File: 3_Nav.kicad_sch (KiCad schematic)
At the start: 36 parts, among them J401 GNSS, Q401 Q_NMOS, SW401 SW_Push, SW402 SW_Push, U401 STM32F446VETx, Y401 YXC YSX321SL

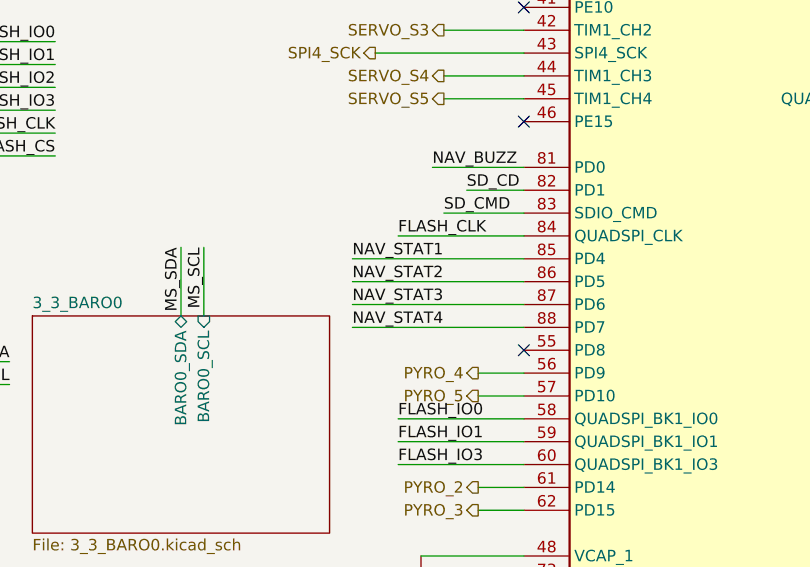
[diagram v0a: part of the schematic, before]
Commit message: Continued laying out traces
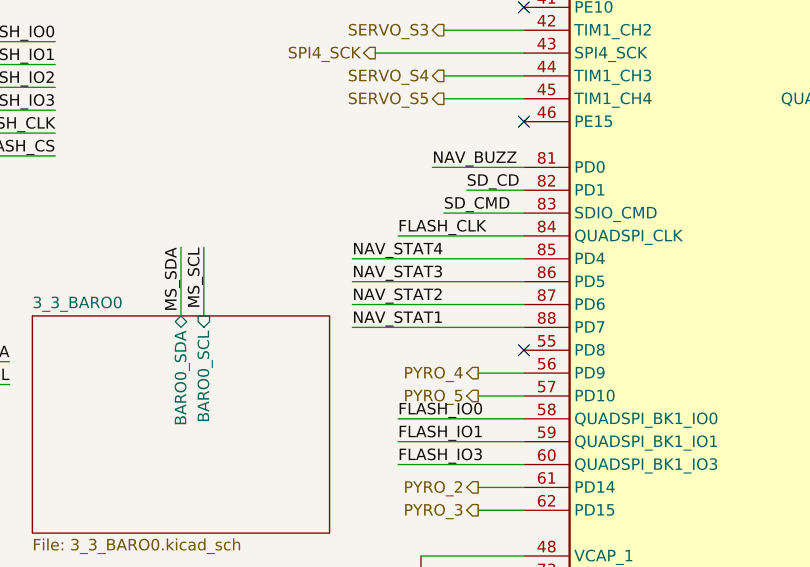
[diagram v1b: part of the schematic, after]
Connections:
- net NAV_STAT1: now also U401.88 (PD7); no longer U401.85 (PD4)
- net NAV_STAT2: now also U401.87 (PD6); no longer U401.86 (PD5)
- net NAV_STAT3: now also U401.86 (PD5); no longer U401.87 (PD6)
- net NAV_STAT4: now also U401.85 (PD4); no longer U401.88 (PD7)
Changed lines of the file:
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@@
 		)
 	)
-	(label "NAV_STAT1"
+	(label "NAV_STAT4"
 		(at 95.25 129.54 0)
 		(effects
@@
 		)
 	)
-	(label "NAV_STAT4"
+	(label "NAV_STAT1"
 		(at 95.25 137.16 0)
 		(effects
@@
 		)
 	)
-	(label "NAV_STAT2"
+	(label "NAV_STAT3"
 		(at 95.25 132.08 0)
 		(effects
@@
 		)
 	)
-	(label "NAV_STAT3"
+	(label "NAV_STAT2"
 		(at 95.25 134.62 0)
 		(effects

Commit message: Major changes
Updated schematic for better power delivery
Changed 3.3V supply to buck converter instead of LDO due to heat
Deleted the entire PCB, redoing the whole thing due to problems in
laying traces that made some connections impossible to make
Also updated README to reflect these changes
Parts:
- added FB402: FerriteBead, Inductor_SMD:L_0603_1608Metric, symbol Device:FerriteBead
- SW401, SW402: footprint Button_Switch_THT:SW_PUSH_6mm -> Button_Switch_SMD:SW_SPST_TS-1088-xR020
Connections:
- net +3.3VA is gone; now on net +3.3V: J401.4 (Pin_4)
- net +3.3V: now also FB402.2; no longer U401.22 (VDDA)
- new net: FB402.1, U401.22 (VDDA)
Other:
- moved on the sheet: C409, C410, C411, C412, C413, C414, C415, C416

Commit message: Finished most of component re-placement
Began laying tracks for important connections
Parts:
- removed R403: 0R, Resistor_SMD:R_0603_1608Metric, symbol Device:R
- C401, C402: value 12p -> 20p
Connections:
- net +3.3V: no longer C416.1
- net OSC_OUT: now also U401.13 (PH1)
- net at FB402.1, U401.22 (VDDA): now also C416.1
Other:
- note added: "12 pF load capacitance"
- note removed: "9 pF load capacitance"
- moved on the sheet: C416, FB402

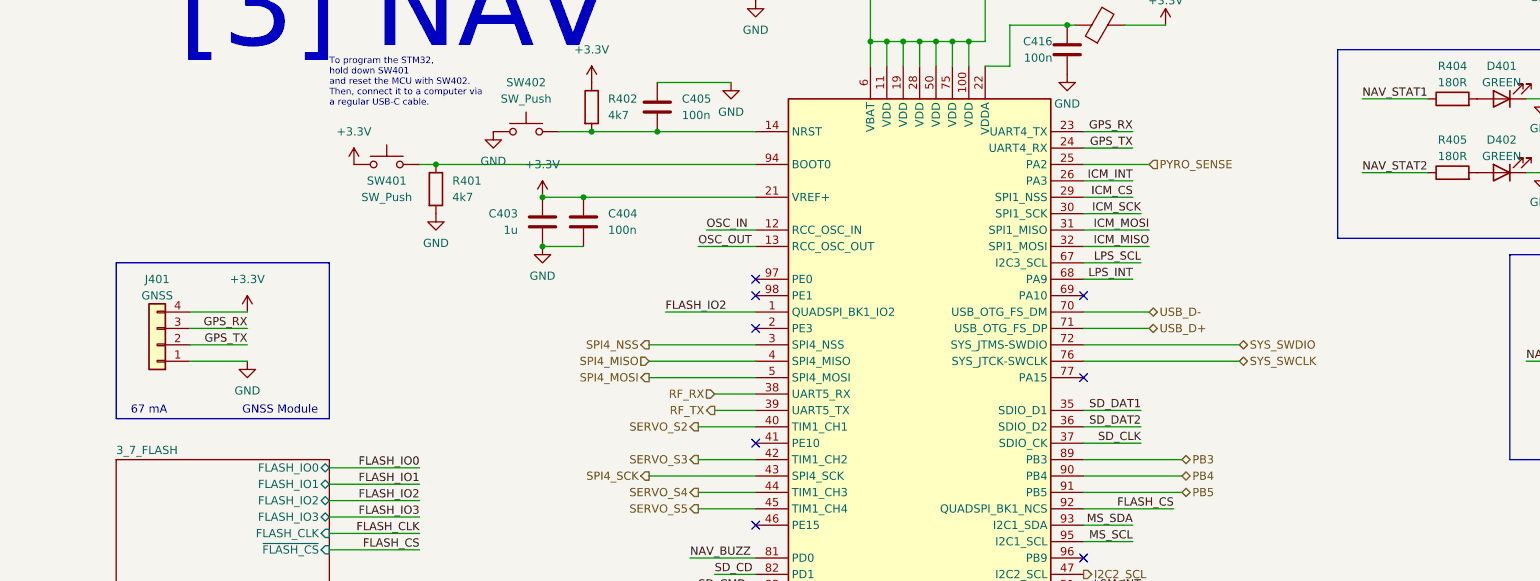
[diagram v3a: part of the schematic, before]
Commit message: Added more power (3.3V) headers for more powering peripherals
Continued laying out tracks
Revised order of connections to pyrochannel mux for easier routing
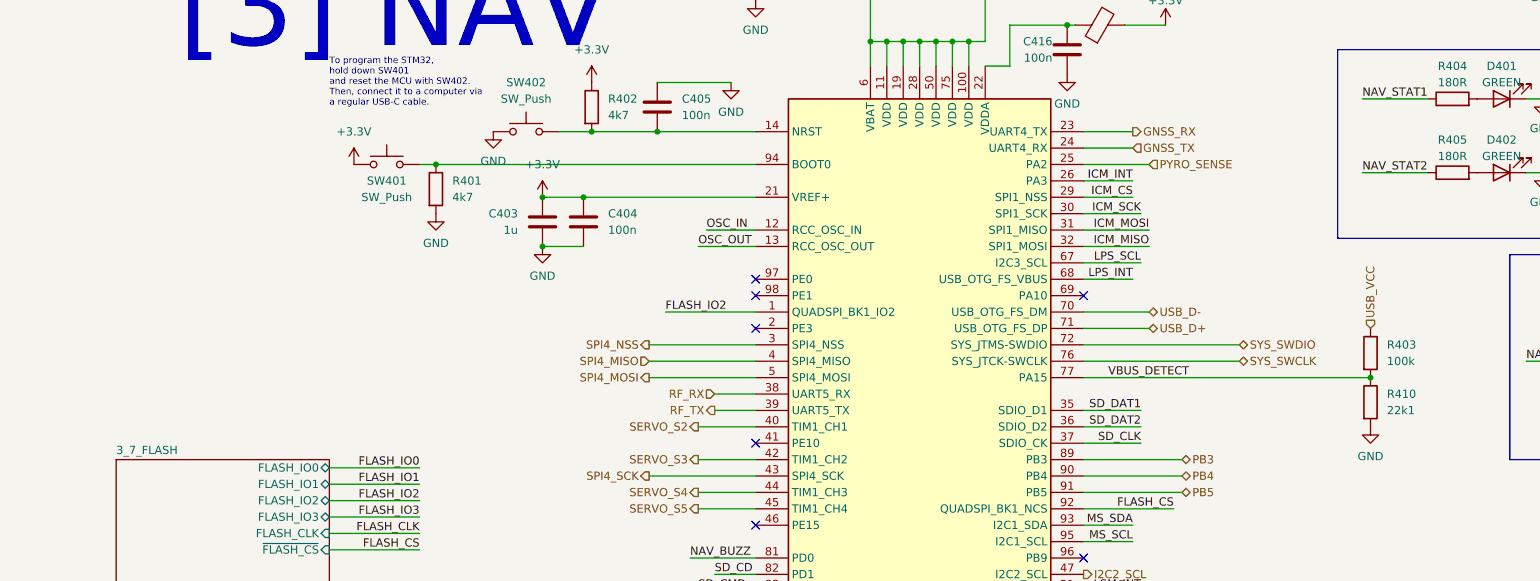
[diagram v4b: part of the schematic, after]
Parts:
- removed J401: GNSS, Connector_JST:JST_XH_B4B-XH-A_1x04_P2.50mm_Vertical, symbol Connector_Generic:Conn_01x04
- added R403: 100k, Resistor_SMD:R_0603_1608Metric, symbol Device:R
- added R410: 22k1, Resistor_SMD:R_0603_1608Metric, symbol Device:R
- C408: footprint Capacitor_SMD:C_0603_1608Metric -> Capacitor_SMD:C_0805_2012Metric
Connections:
- net GND: now also R410.2
- net VBUS_DETECT: now reaches U401.77 (PA15)
- net VBUS_DETECT: now also R403.2, R410.1
- net GPS_RX renamed GNSS_RX
- net GPS_TX renamed GNSS_TX
- new net USB_VCC: R403.1
- no-connect marks 13 -> 12
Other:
- note removed: "67 mA"
- note removed: "GNSS Module"
